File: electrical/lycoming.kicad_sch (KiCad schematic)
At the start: 26 parts

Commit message: Updated from learnings from N78HR
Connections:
- net Earth: no longer SFLY_LEFT. (PLEAD), SFLY_LEFT_SW.1 (A)
- new net: SFLY_LEFT. (PLEAD), SFLY_LEFT_SW.1 (A)
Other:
- moved on the sheet: SFLY_LEFT_SW
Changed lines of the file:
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@@
 	(title_block
 		(title "Lycoming")
-		(date "2025-11-01")
+		(date "2025-11-19")
 		(rev "1.1")
 	)
@@
 	)
 	(junction
-		(at 109.22 151.13)
-		(diameter 0)
-		(color 0 0 0 0)
-	)
-	(junction
-		(at 31.75 72.39)
-		(diameter 0)
-		(color 0 0 0 0)
-	)
-	(junction
 		(at 109.22 170.18)
 		(diameter 0)
@@
 	(wire
 		(pts
-			(xy 17.78 72.39) (xy 31.75 72.39)
-		)
-		(stroke
-			(width 0)
-			(type default)
-		)
-	)
-	(wire
-		(pts
 			(xy 62.23 97.79) (xy 109.22 97.79)
 		)
@@
 	(wire
 		(pts
-			(xy 71.12 157.48) (xy 110.49 157.48)
+			(xy 71.12 153.67) (xy 110.49 153.67)
 		)
 		(stroke
@@
 	(wire
 		(pts
-			(xy 109.22 154.94) (xy 109.22 151.13)
-		)
-		(stroke
-			(width 0)
-			(type default)
-		)
-	)
-	(wire
-		(pts
 			(xy 64.77 43.18) (xy 64.77 50.8)
 		)
@@
 	(wire
 		(pts
-			(xy 17.78 72.39) (xy 17.78 151.13)
-		)
-		(stroke
-			(width 0)
-			(type default)
-		)
-	)
-	(wire
-		(pts
 			(xy 43.18 25.4) (xy 50.8 25.4)
 		)
@@
 	(wire
 		(pts
-			(xy 110.49 153.67) (xy 110.49 157.48)
-		)
-		(stroke
-			(width 0)
-			(type default)
-		)
-	)
-	(wire
-		(pts
 			(xy 73.66 59.69) (xy 82.55 59.69)
 		)
@@
 	(wire
 		(pts
-			(xy 55.88 157.48) (xy 60.96 157.48)
+			(xy 55.88 153.67) (xy 60.96 153.67)
 		)
 		(stroke
@@
 	(wire
 		(pts
-			(xy 55.88 154.94) (xy 55.88 157.48)
+			(xy 55.88 151.13) (xy 55.88 153.67)
 		)
 		(stroke
@@
 	(wire
 		(pts
-			(xy 55.88 154.94) (xy 109.22 154.94)
+			(xy 55.88 151.13) (xy 109.22 151.13)
 		)
 		(stroke
@@
 		(pts
 			(xy 149.86 66.04) (xy 149.86 77.47)
-		)
-		(stroke
-			(width 0)
-			(type default)
-		)
-	)
-	(wire
-		(pts
-			(xy 17.78 151.13) (xy 109.22 151.13)
 		)
 		(stroke
@@
 	(symbol
 		(lib_id "Switch:SW_SPST")
-		(at 66.04 157.48 0)
+		(at 66.04 153.67 0)
 		(unit 1)
 		(exclude_from_sim no)
@@
 		(dnp no)
 		(property "Reference" "SFLY_LEFT_SW"
-			(at 66.294 160.274 0)
+			(at 66.294 156.464 0)
 			(effects
 				(font
@@
 		)
 		(property "Value" "~"
+			(at 66.04 149.86 0)
+			(effects
+				(font
+					(size 1.27 1.27)
+				)
+				(hide yes)
+			)
+		)
+		(property "Footprint" ""
 			(at 66.04 153.67 0)
 			(effects
@@
 			)
 		)
-		(property "Footprint" ""
-			(at 66.04 157.48 0)
-			(effects
-				(font
-					(size 1.27 1.27)
-				)
-				(hide yes)
-			)
-		)
 		(property "Datasheet" "~"
-			(at 66.04 157.48 0)
+			(at 66.04 153.67 0)
 			(effects
 				(font
@@
 		)
 		(property "Description" ""
-			(at 66.04 157.48 0)
-			(effects
-				(font
+			(at 66.04 153.67 0)
+			(effects
+				(font

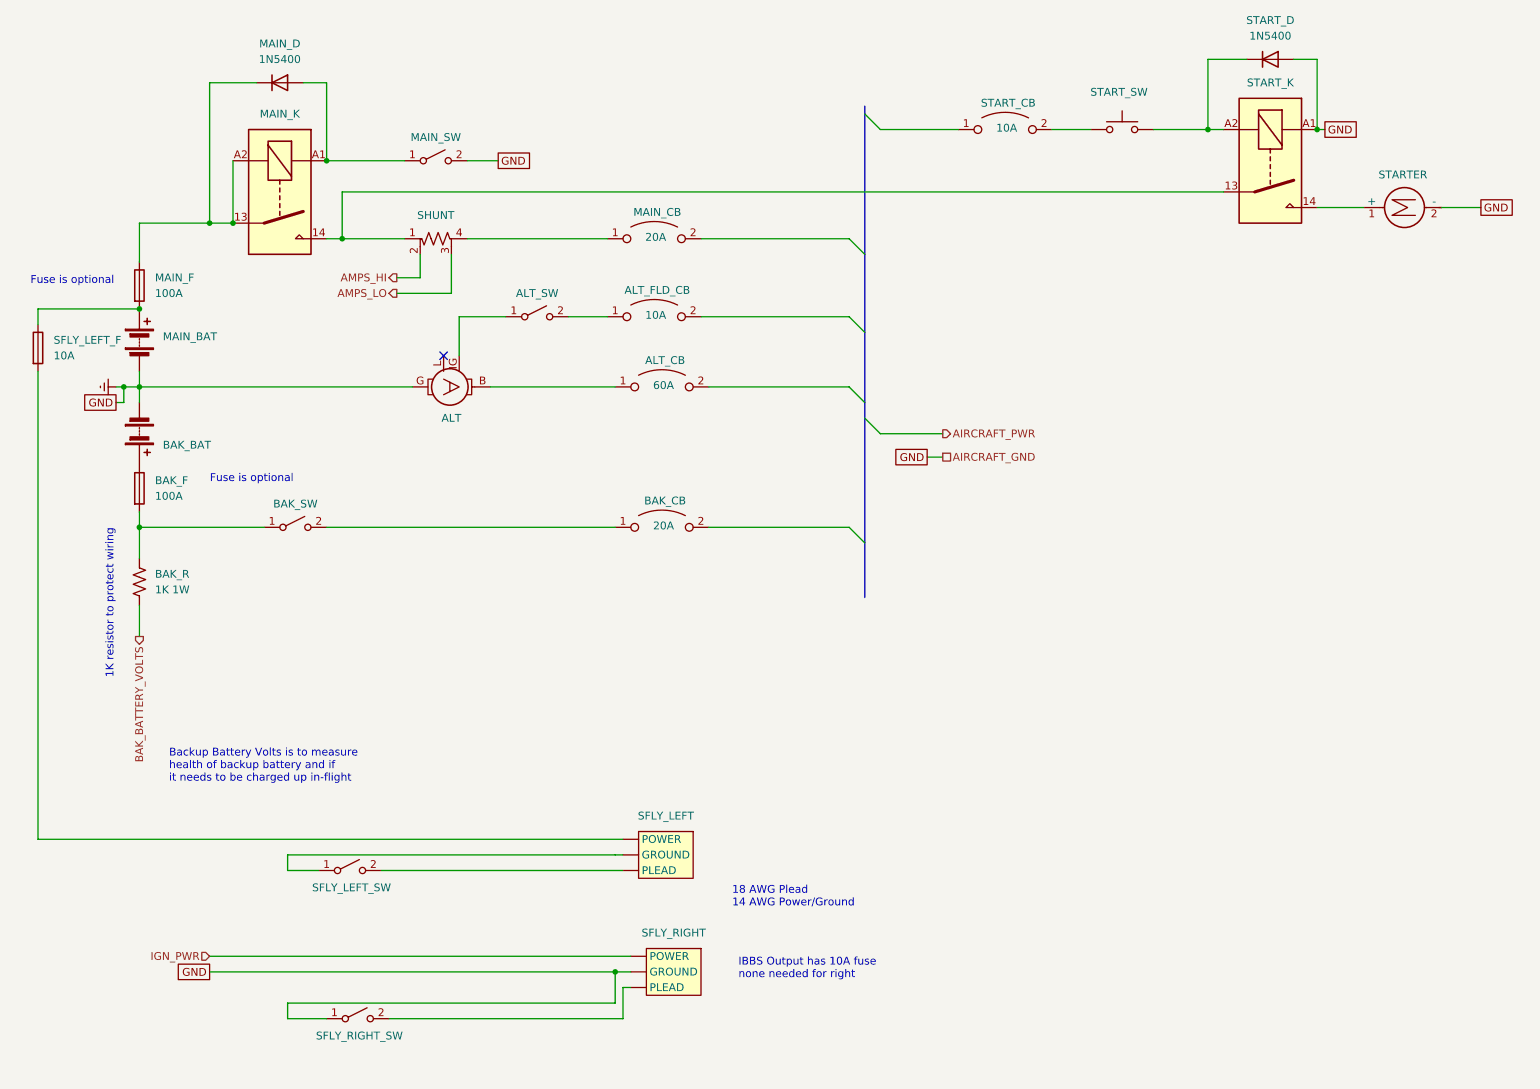
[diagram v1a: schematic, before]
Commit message: Went through and changed a lot from discussions and tradeoffs. Added GTX 330, rmemoved Connext from GDU and added to GPS 175 from GDL 52. Added relay for smoke and to not use GAD 27. Added Tach sensor for SureFly. Added carb heat. Added connectors to run panel disconnected.
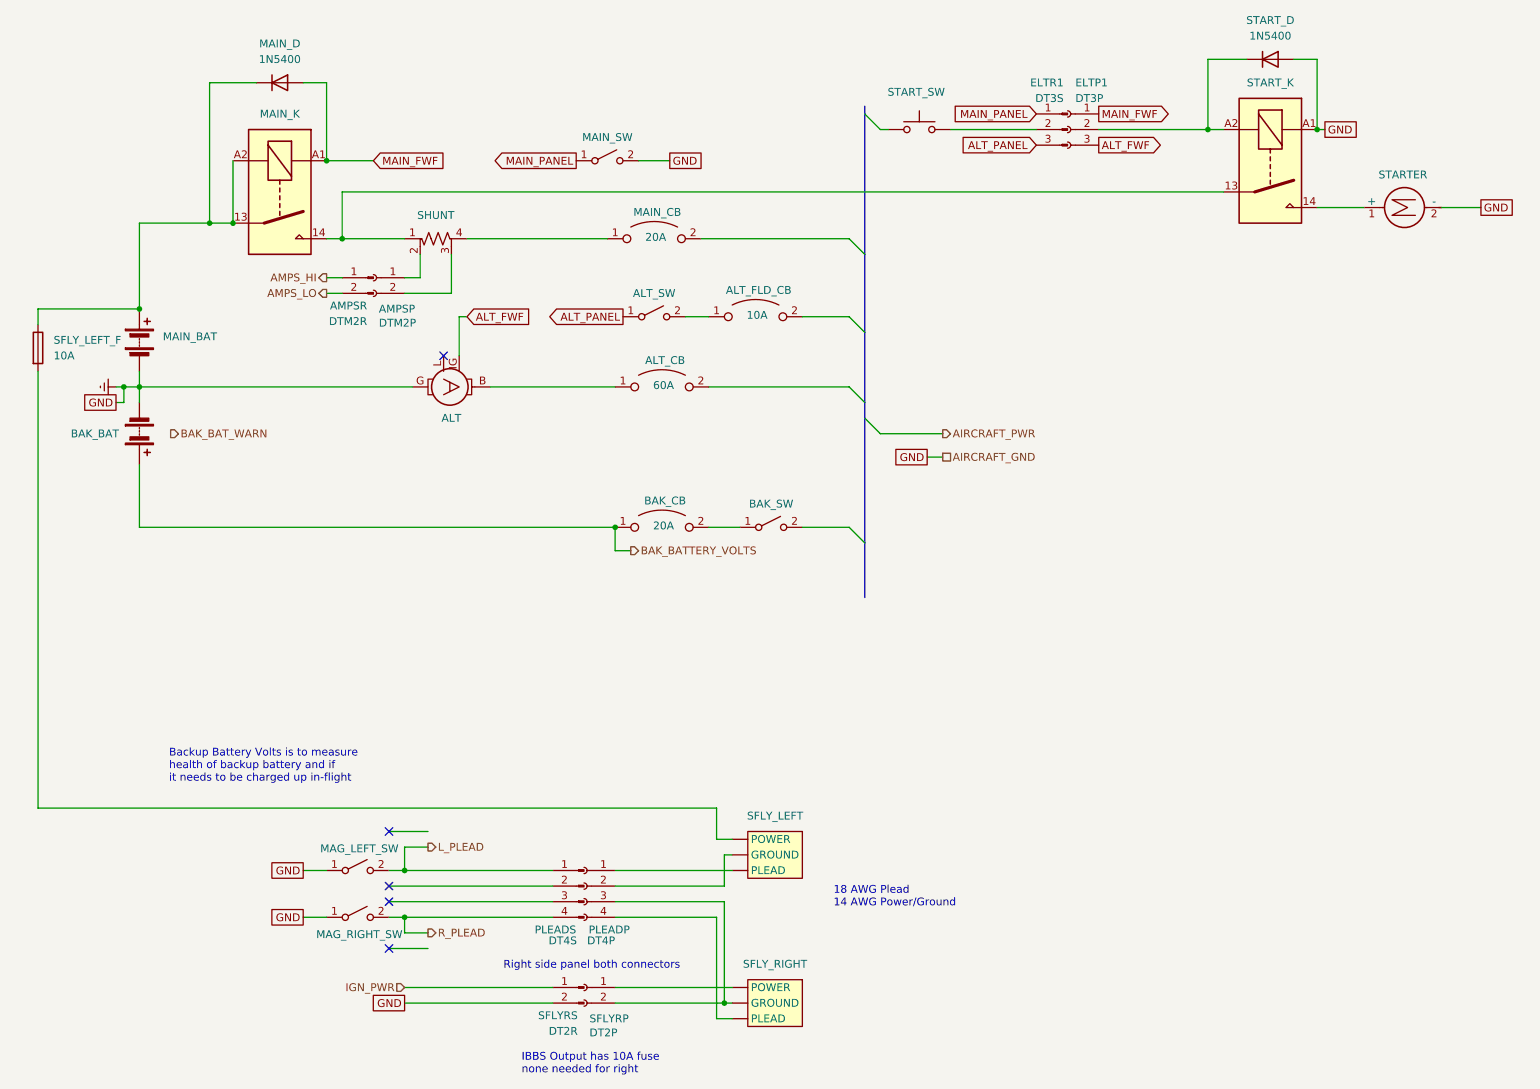
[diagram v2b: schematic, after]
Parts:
- removed BAK_F, MAIN_F: 100A, symbol Device:Fuse
- removed BAK_R: 1K 1W, symbol Device:R_US
- removed START_CB: 10A, symbol Device:CircuitBreaker_1P_US
- added AMPSP: DTM2P, symbol Connector:Conn_01x02_Socket
- added AMPSR: DTM2R, symbol Connector:Conn_01x02_Pin
- added ELTP1: DT3P, symbol Connector:Conn_01x03_Socket
- added ELTR1: DT3S, symbol Connector:Conn_01x03_Pin
- added PLEADP: DT4P, symbol Connector:Conn_01x04_Socket
- added PLEADS: DT4S, symbol Connector:Conn_01x04_Pin
- added SFLYRP: DT2P, symbol Connector:Conn_01x02_Socket
- added SFLYRS: DT2R, symbol Connector:Conn_01x02_Pin
- renumbered SFLY_LEFT_SW to MAG_LEFT_SW, SFLY_RIGHT_SW to MAG_RIGHT_SW
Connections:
- net AMPS_HI: now also AMPSR.1 (Pin_1); no longer SHUNT.2
- net AMPS_LO: now also AMPSR.2 (Pin_2); no longer SHUNT.3
- net BAK_BATTERY_VOLTS: now also BAK_BAT.1 (+), BAK_CB.1
- net Earth: now also MAG_LEFT_SW.1 (A), SFLYRS.2 (Pin_2); no longer SFLY_RIGHT. (PLEAD)
- net IGN_PWR: now also SFLYRS.1 (Pin_1); no longer SFLY_RIGHT. (PLEAD)
- net at SFLY_RIGHT. (PLEAD): now also SFLYRP.1 (Pin_1); no longer MAG_RIGHT_SW.2 (B)
- net at SFLY_LEFT. (PLEAD): now also SFLY_LEFT_F.2; no longer MAG_LEFT_SW.1 (A)
- net L_PLEAD: now reaches MAG_LEFT_SW.2 (B)
- net L_PLEAD: now also PLEADS.1 (Pin_1); no longer SFLY_LEFT. (PLEAD)
- net at MAIN_D.1 (K), MAIN_K.13, MAIN_K.A2: now also MAIN_BAT.1 (+), SFLY_LEFT_F.1
- net MAIN_FWF: now reaches MAIN_D.2 (A), MAIN_K.A1
- net MAIN_FWF: now also ELTP1.1 (Pin_1); no longer MAIN_SW.1 (A)
- net at START_D.1 (K), START_K.A2: now also ELTP1.2 (Pin_2); no longer START_SW.2
- net at BAK_SW.1 (A): now also BAK_CB.2
- net ALT_FWF: now reaches ALT.IG
- net ALT_FWF: now also ELTP1.3 (Pin_3); no longer ALT_SW.1 (A)
- net at BAK_SW.2 (B): no longer BAK_CB.1
- new net: PLEADP.3 (Pin_3), SFLYRP.2 (Pin_2), SFLY_RIGHT. (PLEAD)
- new net: PLEADP.4 (Pin_4), SFLY_RIGHT. (PLEAD)
- new net: ELTR1.2 (Pin_2), START_SW.2
- new net: PLEADP.1 (Pin_1), SFLY_LEFT. (PLEAD)
- new net: PLEADP.2 (Pin_2), SFLY_LEFT. (PLEAD)
- new net: AMPSP.1 (Pin_1), SHUNT.2
- new net: AMPSP.2 (Pin_2), SHUNT.3
- new net ALT_PANEL: ALT_SW.1 (A), ELTR1.3 (Pin_3)
- new net MAIN_PANEL: ELTR1.1 (Pin_1), MAIN_SW.1 (A)
- new net R_PLEAD: MAG_RIGHT_SW.2 (B), PLEADS.4 (Pin_4)
- no-connect marks 1 -> 5
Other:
- note added: "Right side panel both connectors"
- note removed: "1K resistor to protect wiring"
- note removed: "Fuse is optional"
- moved on the sheet: ALT_FLD_CB, ALT_SW, BAK_SW, MAG_LEFT_SW, MAG_RIGHT_SW, MAIN_SW, SFLY_LEFT, SFLY_RIGHT, START_SW

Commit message: Added AWG wires.
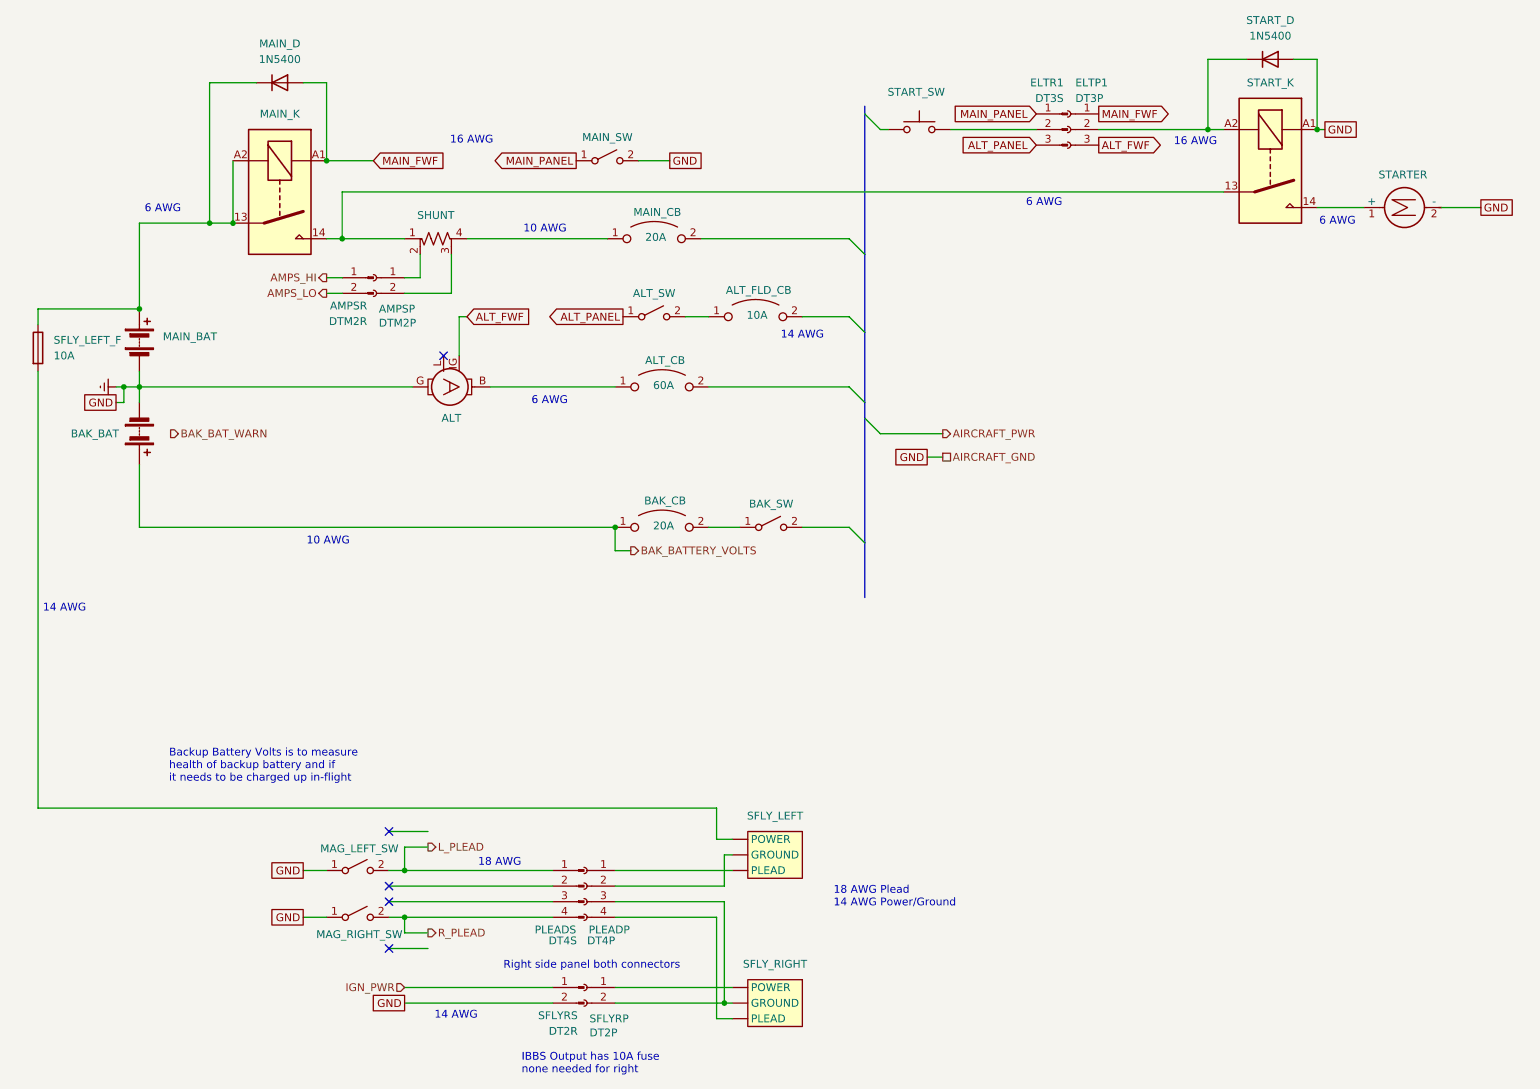
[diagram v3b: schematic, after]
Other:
- note added: "10 AWG"
- note added: "14 AWG"
- note added: "16 AWG"
- note added: "18 AWG"
- note added: "6 AWG"
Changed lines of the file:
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@@
 		(title "Lycoming")
 		(date "2025-12-24")
-		(rev "1.2")
+		(rev "1.2.1")
 	)
 	(text "Right side panel both connectors"
 		(exclude_from_sim no)
 		(at 105.41 169.164 0)
+		(effects
+			(font
+				(size 1.27 1.27)
+			)
+		)
+	)
+	(text "14 AWG"
+		(exclude_from_sim no)
+		(at 139.7 66.548 0)
+		(effects
+			(font
+				(size 1.27 1.27)
+			)
+		)
+	)
+	(text "6 AWG"
+		(exclude_from_sim no)
+		(at 98.552 77.216 0)
+		(effects
+			(font
+				(size 1.27 1.27)
+			)
+		)
+	)
+	(text "6 AWG"
+		(exclude_from_sim no)
+		(at 226.822 48.006 0)
+		(effects
+			(font
+				(size 1.27 1.27)
+			)
+		)
+	)
+	(text "16 AWG"
+		(exclude_from_sim no)
+		(at 85.852 34.798 0)
+		(effects
+			(font
+				(size 1.27 1.27)
+			)
+		)
+	)
+	(text "16 AWG"
+		(exclude_from_sim no)
+		(at 203.708 35.052 0)
+		(effects
+			(font
+				(size 1.27 1.27)
+			)
+		)
+	)
+	(text "18 AWG"
+		(exclude_from_sim no)
+		(at 90.424 152.4 0)
+		(effects
+			(font
+				(size 1.27 1.27)
+			)
+		)
+	)
+	(text "6 AWG"
+		(exclude_from_sim no)
+		(at 179.07 44.958 0)
 		(effects
 			(font
@@
 		)
 	)
+	(text "14 AWG"
+		(exclude_from_sim no)
+		(at 19.558 110.998 0)
+		(effects
+			(font
+				(size 1.27 1.27)
+			)
+		)
+	)
+	(text "10 AWG"
+		(exclude_from_sim no)
+		(at 97.79 49.276 0)
+		(effects
+			(font
+				(size 1.27 1.27)
+			)
+		)
+	)
 	(text "18 AWG Plead\n14 AWG Power/Ground"
 		(exclude_from_sim no)
@@
 		)
 	)
+	(text "10 AWG"
+		(exclude_from_sim no)
+		(at 62.484 100.076 0)
+		(effects
+			(font
+				(size 1.27 1.27)
+			)
+		)
+	)
+	(text "6 AWG"
+		(exclude_from_sim no)
+		(at 35.56 45.974 0)
+		(effects
+			(font
+				(size 1.27 1.27)
+			)
+		)
+	)
+	(text "14 AWG"
+		(exclude_from_sim no)
+		(at 83.312 177.292 0)
+		(effects
+			(font
+				(size 1.27 1.27)
+			)
+		)
+	)

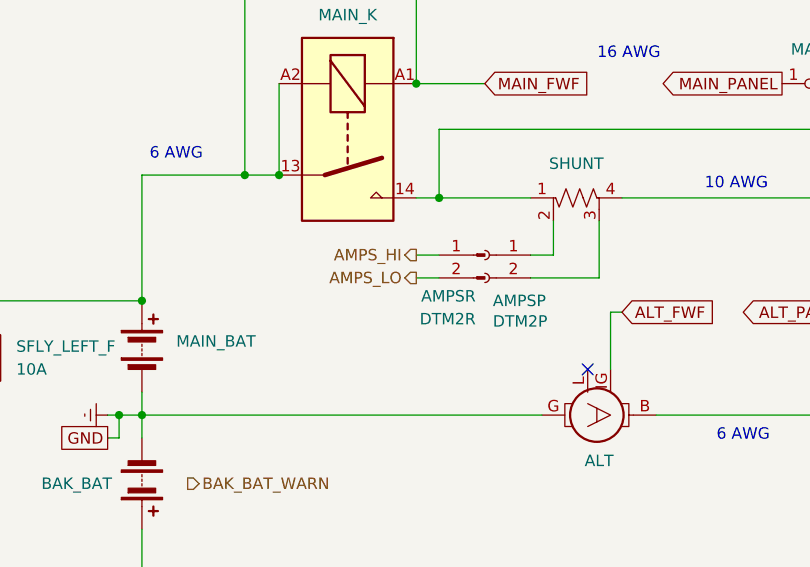
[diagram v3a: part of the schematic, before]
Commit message: Added beacon and added colors for flaps
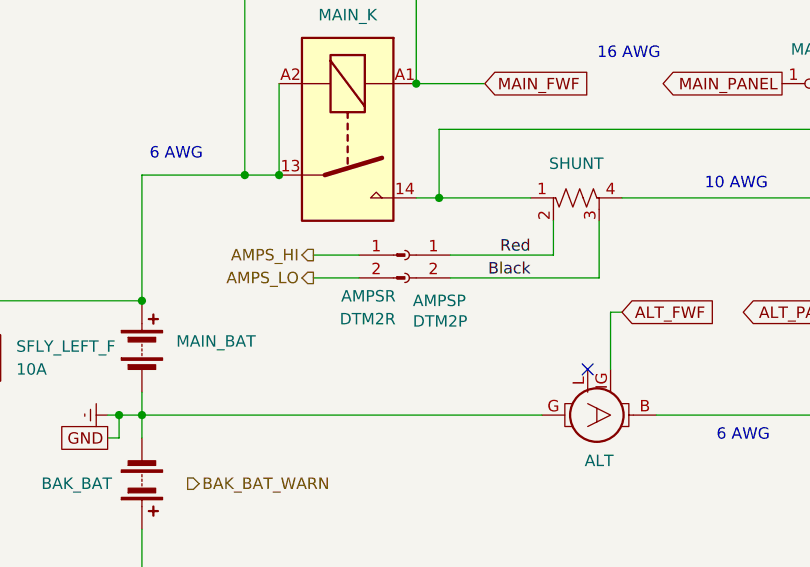
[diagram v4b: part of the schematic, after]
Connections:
- net Red: now reaches AMPSP.1 (Pin_1), SHUNT.2
- net Black: now reaches AMPSP.2 (Pin_2), SHUNT.3
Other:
- moved on the sheet: AMPSP, AMPSR
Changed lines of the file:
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@@
 	(title_block
 		(title "Lycoming")
-		(date "2025-12-24")
-		(rev "1.2.1")
+		(date "2026-01-01")
+		(rev "1.2.3")
 	)
 	(text "Right side panel both connectors"
@@
 	(wire
 		(pts
-			(xy 74.93 57.15) (xy 77.47 57.15)
+			(xy 66.04 57.15) (xy 77.47 57.15)
 		)
 		(stroke
@@
 	(wire
 		(pts
-			(xy 74.93 59.69) (xy 82.55 59.69)
+			(xy 66.04 59.69) (xy 82.55 59.69)
 		)
 		(stroke
@@
 	(wire
 		(pts
-			(xy 62.23 57.15) (xy 64.77 57.15)
+			(xy 50.8 57.15) (xy 55.88 57.15)
 		)
 		(stroke
@@
 	(wire
 		(pts
-			(xy 62.23 59.69) (xy 64.77 59.69)
+			(xy 50.8 59.69) (xy 55.88 59.69)
 		)
 		(stroke
@@
 		)
 	)
+	(label "Red"
+		(at 74.93 57.15 180)
+		(effects
+			(font
+				(size 1.27 1.27)
+			)
+			(justify right bottom)
+		)
+	)
+	(label "Black"
+		(at 74.93 59.69 180)
+		(effects
+			(font
+				(size 1.27 1.27)
+			)
+			(justify right bottom)
+		)
+	)
 	(global_label "GND"
 		(shape passive)
@@
 	(hierarchical_label "AMPS_HI"
 		(shape output)
-		(at 62.23 57.15 180)
+		(at 50.8 57.15 180)
 		(effects
 			(font
@@
 	(hierarchical_label "AMPS_LO"
 		(shape output)
-		(at 62.23 59.69 180)
+		(at 50.8 59.69 180)
 		(effects
 			(font
@@
 	(symbol
 		(lib_id "Connector:Conn_01x02_Pin")
-		(at 69.85 57.15 0)
+		(at 60.96 57.15 0)
 		(mirror y)
 		(unit 1)
@@
 		(dnp no)
 		(property "Reference" "AMPSR"
-			(at 68.834 61.722 0)
+			(at 59.944 61.722 0)
 			(effects
 				(font
@@
 		)
 		(property "Value" "DTM2R"
-			(at 68.834 64.262 0)
+			(at 59.944 64.262 0)
 			(effects
 				(font
@@
 		)
 		(property "Footprint" ""
-			(at 69.85 57.15 0)
+			(at 60.96 57.15 0)
 			(effects
 				(font
@@
 		)
 		(property "Datasheet" "~"
-			(at 69.85 57.15 0)
+			(at 60.96 57.15 0)
 			(effects
 				(font
@@
 		)
 		(property "Description" "Generic connector, single row, 01x02, script generated"
-			(at 69.85 57.15 0)
+			(at 60.96 57.15 0)
 			(effects
 				(font
@@
 	(symbol
 		(lib_id "Connector:Conn_01x02_Socket")
-		(at 69.85 57.15 0)
+		(at 60.96 57.15 0)
 		(mirror y)
 		(unit 1)
@@
 		(dnp no)
 		(property "Reference" "AMPSP"
-			(at 70.739 62.23 0)
+			(at 61.849 62.23 0)
 			(effects
 				(font
@@
 		)
 		(property "Value" "DTM2P"
-			(at 70.739 64.516 0)
+			(at 61.849 64.516 0)
 			(effects
 				(font
@@
 		)
 		(property "Footprint" ""
-			(at 69.85 57.15 0)
+			(at 60.96 57.15 0)
 			(effects
 				(font
@@
 		)
 		(property "Datasheet" "~"
-			(at 69.85 57.15 0)
+			(at 60.96 57.15 0)
 			(effects
 				(font
@@
 		)
 		(property "Description" "Generic connector, single row, 01x02, script generated"
-			(at 69.85 57.15 0)
+			(at 60.96 57.15 0)
 			(effects
 				(font
